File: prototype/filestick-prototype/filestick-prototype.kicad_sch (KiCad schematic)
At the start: 60 parts, among them J1 DIN-5, J2 DIN-5, J3 GPIO header 1, J4 UART header, J5 GPIO header 2, J6 SPI header, Q1 2N7002, Q2 2N7002, Q3 2N7002, Q4 2N7002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

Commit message: fix prototype PCB errors
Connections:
- net GND: now also U4.42 (GND); no longer U4.41 (GND)
- net MISO: now also J6.6 (Pin_6), U4.45 (GPIO17_MISO); no longer J6.7 (Pin_7), U4.46 (GPIO17_MISO)
- net MOSI: now also J6.7 (Pin_7), U4.46 (GPIO14_MOSI); no longer J6.6 (Pin_6), U4.45 (GPIO14_MOSI)
- net at TP3.1 (Pin_1): now also U4.41 (CLK_12MHz); no longer U4.42 (CLK_12MHz)
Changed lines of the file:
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@@
-    (stroke (width 0) (type default) (color 0 0 0 0))
-  )
-  (wire (pts (xy 316.23 162.56) (xy 316.23 154.94))
     (stroke (width 0) (type default) (color 0 0 0 0))
   )
@@
     (stroke (width 0) (type default) (color 0 0 0 0))
   )
+  (wire (pts (xy 292.1 158.75) (xy 314.96 158.75))
+    (stroke (width 0) (type default) (color 0 0 0 0))
+  )
   (wire (pts (xy 298.45 215.9) (xy 292.1 215.9))
     (stroke (width 0) (type default) (color 0 0 0 0))
@@
     (stroke (width 0) (type default) (color 0 0 0 0))
   )
-  (wire (pts (xy 321.31 157.48) (xy 327.66 157.48))
-    (stroke (width 0) (type default) (color 0 0 0 0))
-  )
   (wire (pts (xy 359.41 177.8) (xy 365.76 177.8))
     (stroke (width 0) (type default) (color 0 0 0 0))
@@
     (stroke (width 0) (type default) (color 0 0 0 0))
   )
+  (wire (pts (xy 317.5 157.48) (xy 317.5 162.56))
+    (stroke (width 0) (type default) (color 0 0 0 0))
+  )
   (wire (pts (xy 227.33 26.67) (xy 227.33 49.53))
     (stroke (width 0) (type default) (color 0 0 0 0))
@@
     (stroke (width 0) (type default) (color 0 0 0 0))
   )
-  (wire (pts (xy 321.31 158.75) (xy 321.31 157.48))
+  (wire (pts (xy 314.96 154.94) (xy 314.96 158.75))
     (stroke (width 0) (type default) (color 0 0 0 0))
   )
@@
     (stroke (width 0) (type default) (color 0 0 0 0))
   )
-  (wire (pts (xy 316.23 154.94) (xy 327.66 154.94))
-    (stroke (width 0) (type default) (color 0 0 0 0))
-  )
   (wire (pts (xy 81.28 175.26) (xy 81.28 152.4))
     (stroke (width 0) (type default) (color 0 0 0 0))
@@
     (stroke (width 0) (type default) (color 0 0 0 0))
   )
-  (wire (pts (xy 292.1 162.56) (xy 316.23 162.56))
-    (stroke (width 0) (type default) (color 0 0 0 0))
-  )
   (wire (pts (xy 57.15 83.82) (xy 71.12 83.82))
     (stroke (width 0) (type default) (color 0 0 0 0))
@@
     (stroke (width 0) (type default) (color 0 0 0 0))
   )
-  (wire (pts (xy 292.1 158.75) (xy 321.31 158.75))
-    (stroke (width 0) (type default) (color 0 0 0 0))
-  )
   (wire (pts (xy 68.58 185.42) (xy 68.58 180.34))
     (stroke (width 0) (type default) (color 0 0 0 0))
@@
     (stroke (width 0) (type default) (color 0 0 0 0))
   )
+  (wire (pts (xy 292.1 162.56) (xy 317.5 162.56))
+    (stroke (width 0) (type default) (color 0 0 0 0))
+  )
   (wire (pts (xy 110.49 59.69) (xy 105.41 59.69))
     (stroke (width 0) (type default) (color 0 0 0 0))
   )
+  (wire (pts (xy 327.66 157.48) (xy 317.5 157.48))
+    (stroke (width 0) (type default) (color 0 0 0 0))
+  )
   (wire (pts (xy 24.13 80.01) (xy 35.56 80.01))
     (stroke (width 0) (type default) (color 0 0 0 0))
@@
     (stroke (width 0) (type default) (color 0 0 0 0))
   )
+  (wire (pts (xy 314.96 154.94) (xy 327.66 154.94))
+    (stroke (width 0) (type default) (color 0 0 0 0))
+  )
   (wire (pts (xy 219.71 212.09) (xy 250.19 212.09))
     (stroke (width 0) (type default) (color 0 0 0 0))
@@
     (stroke (width 0) (type default) (color 0 0 0 0))
   )
-  (label "MOSI" (at 302.26 162.56 0)
+  (label "MOSI" (at 302.26 158.75 0)
     (effects (font (size 1.27 1.27)) (justify left bottom))
   )
@@
     (effects (font (size 1.27 1.27)) (justify left bottom))
   )
+  (label "MOSI" (at 359.41 180.34 0)
+    (effects (font (size 1.27 1.27)) (justify left bottom))
+  )
   (label "SS3" (at 302.26 177.8 0)
     (effects (font (size 1.27 1.27)) (justify left bottom))
@@
     (effects (font (size 1.27 1.27)) (justify left bottom))
   )
-  (label "MOSI" (at 359.41 182.88 0)
-    (effects (font (size 1.27 1.27)) (justify left bottom))
-  )
   (label "COLLISION_REF_PWM" (at 195.58 58.42 0)
     (effects (font (size 1.27 1.27)) (justify left bottom))
@@
     (effects (font (size 1.27 1.27)) (justify left bottom))
   )
-  (label "MISO" (at 302.26 158.75 0)
-    (effects (font (size 1.27 1.27)) (justify left bottom))
-  )
-  (label "MISO" (at 359.41 180.34 0)
+  (label "MISO" (at 302.26 162.56 0)
     (effects (font (size 1.27 1.27)) (justify left bottom))
   )
@@
     (effects (font (size 1.27 1.27)) (justify left bottom))
   )
+  (label "MISO" (at 359.41 182.88 0)
+    (effects (font (size 1.27 1.27)) (justify left bottom))
+  )

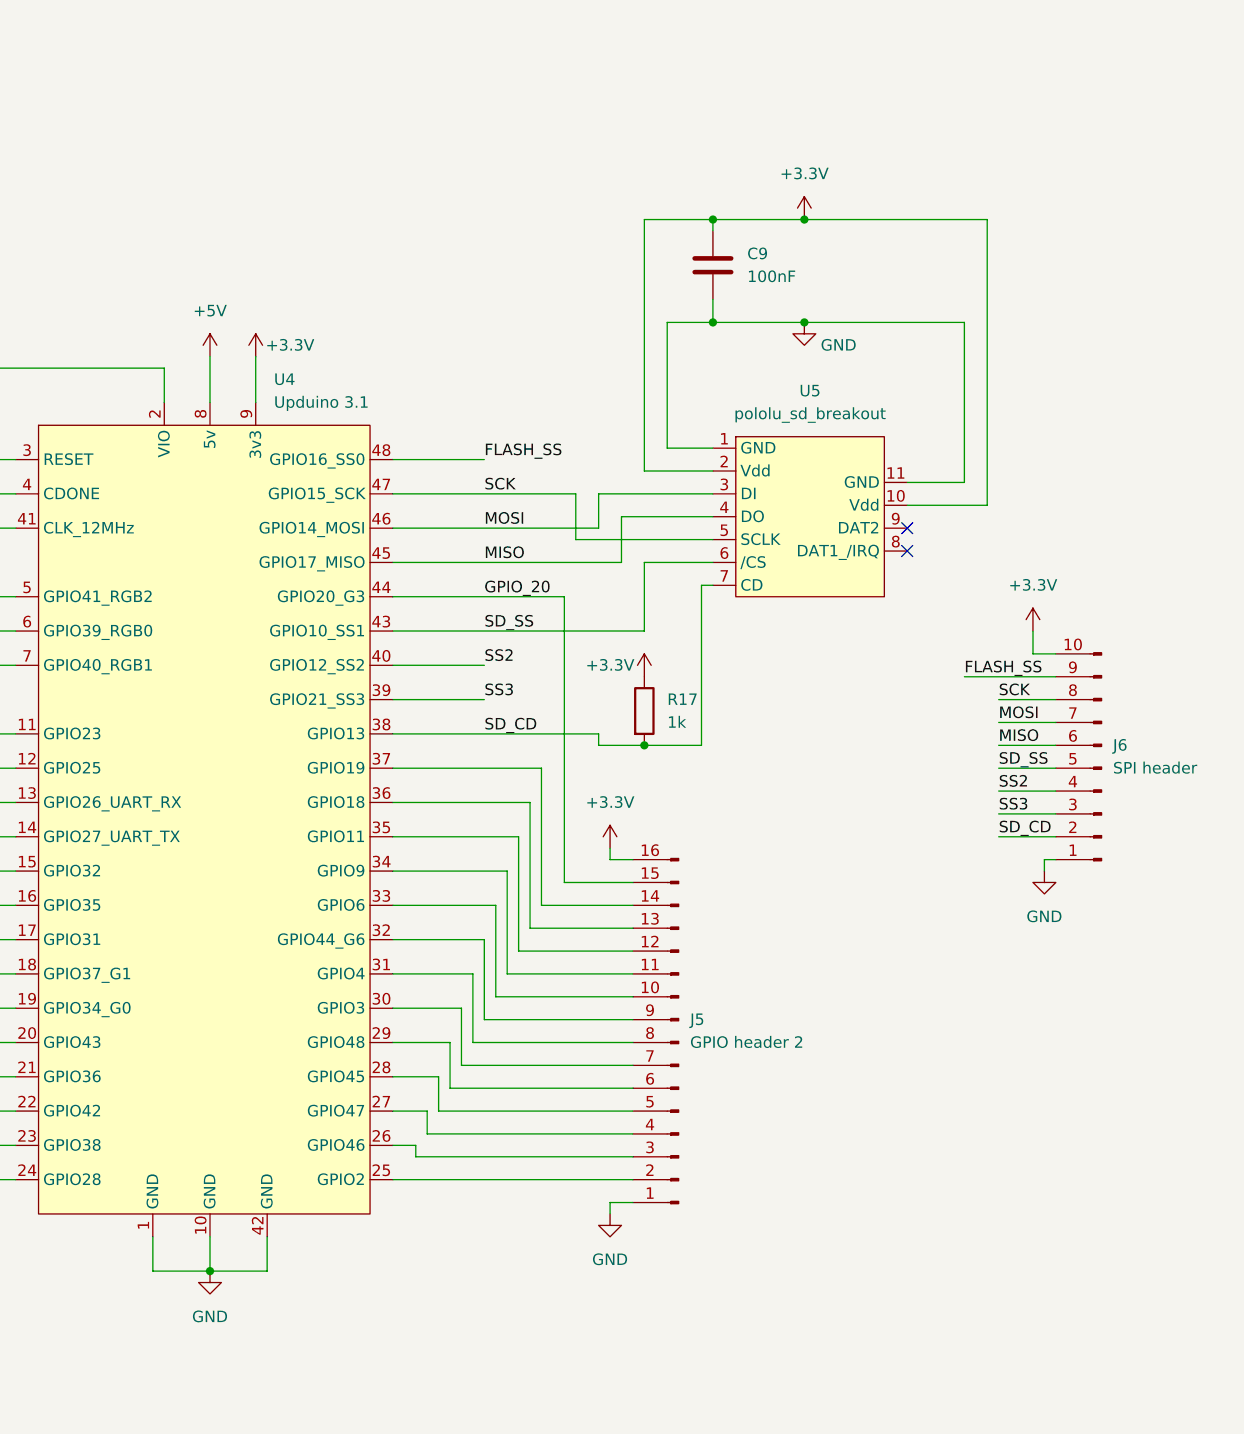
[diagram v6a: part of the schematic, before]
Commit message: Update schematic with dedicated flash spi port
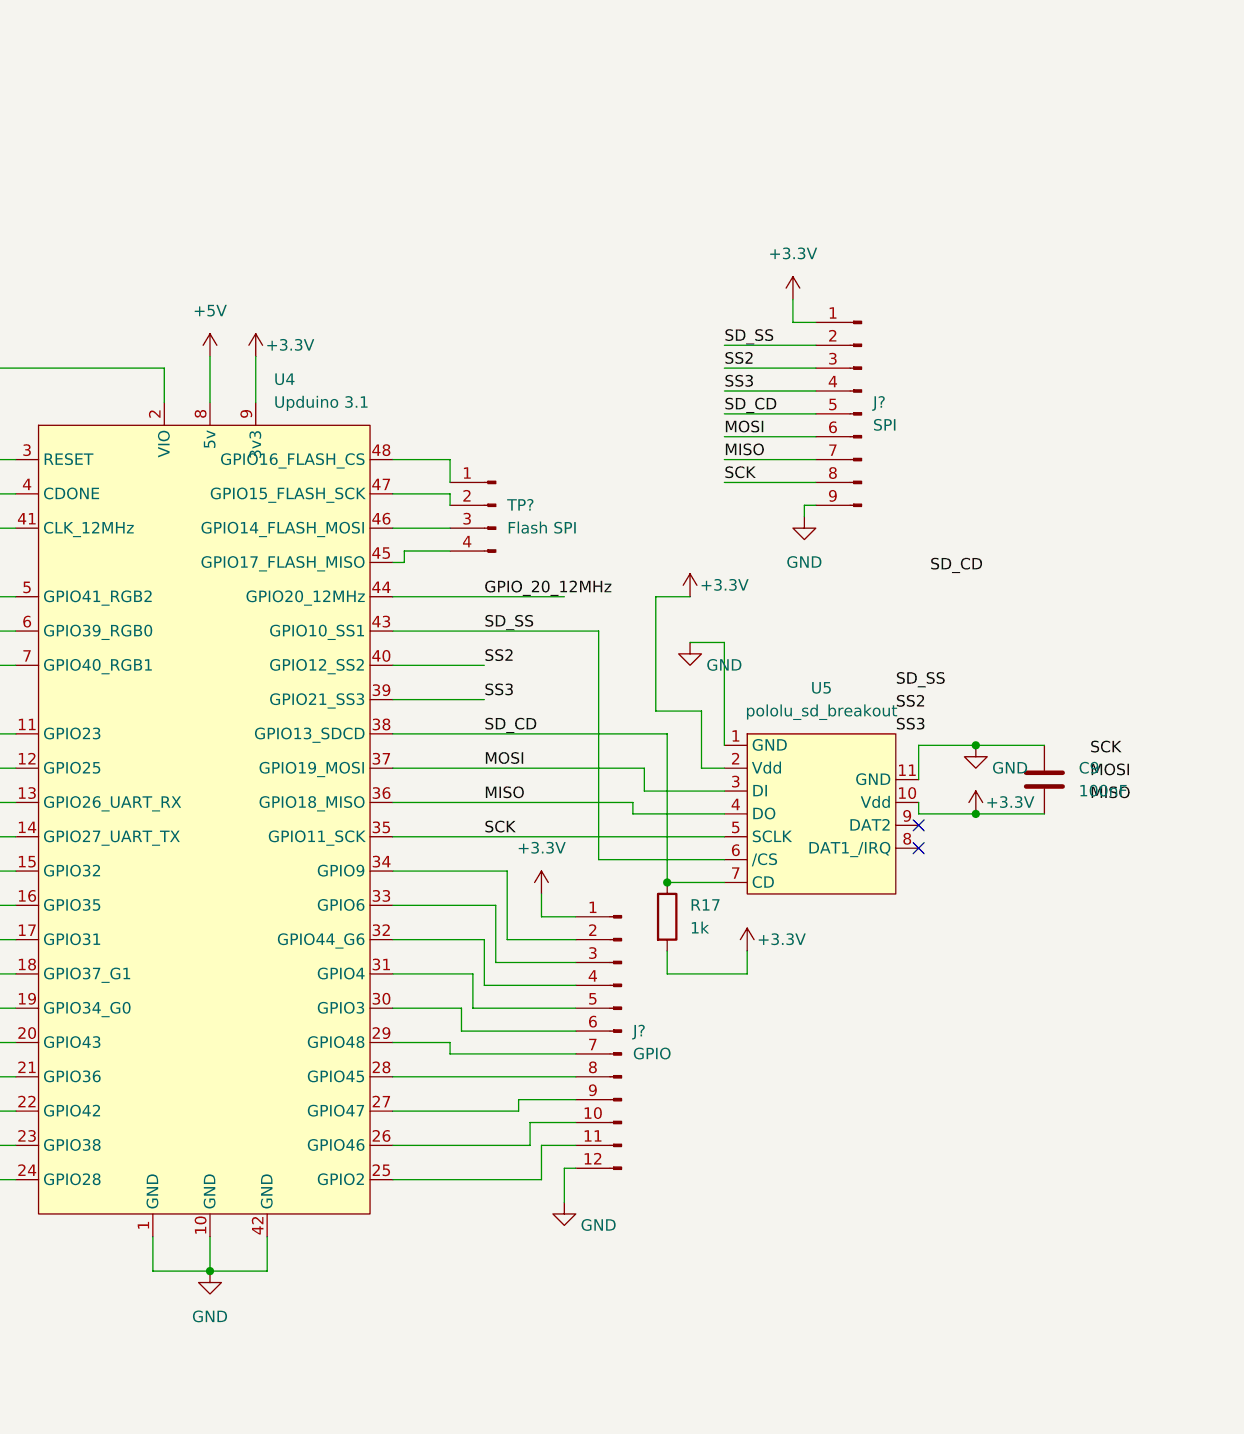
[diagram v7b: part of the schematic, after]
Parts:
- removed J5: GPIO header 2, Connector_PinHeader_2.54mm:PinHeader_1x16_P2.54mm_Vertical, symbol Connector:Conn_01x16_Male
- removed J6: SPI header, Connector_PinHeader_2.54mm:PinHeader_1x10_P2.54mm_Vertical, symbol Connector:Conn_01x10_Male
- added J?: SPI, symbol Connector:Conn_01x09_Male
- added J?: GPIO, symbol Connector:Conn_01x12_Male
- added TP?: Flash SPI, symbol Connector:Conn_01x04_Male
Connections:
- net +3.3V: now also C9.2, R17.2, J?.1 (Pin_1), J?.1 (Pin_1); no longer C9.1, R17.1
- net GND: now also C9.1, J?.12 (Pin_12), J?.9 (Pin_9); no longer C9.2
- net MISO: now also U4.36 (GPIO18_MISO), J?.7 (Pin_7); no longer U4.45 (GPIO17_MISO)
- net MOSI: now also U4.37 (GPIO19_MOSI), J?.6 (Pin_6); no longer U4.46 (GPIO14_MOSI)
- net SCK: now also U4.35 (GPIO11_SCK), J?.8 (Pin_8); no longer U4.47 (GPIO15_SCK)
- net SD_CD: now also R17.1, J?.5 (Pin_5); no longer R17.2
- net SD_SS: now also J?.2 (Pin_2)
- net SS2: now also J?.3 (Pin_3)
- net SS3: now also J?.4 (Pin_4)
- net at U4.25 (GPIO2): now also J?.11 (Pin_11)
- net at U4.26 (GPIO46): now also J?.10 (Pin_10)
- net at U4.27 (GPIO47): now also J?.9 (Pin_9)
- net at U4.28 (GPIO45): now also J?.8 (Pin_8)
- net at U4.29 (GPIO48): now also J?.7 (Pin_7)
- net at U4.30 (GPIO3): now also J?.6 (Pin_6)
- net at U4.31 (GPIO4): now also J?.5 (Pin_5)
- net at U4.32 (GPIO44_G6): now also J?.4 (Pin_4)
- net at U4.33 (GPIO6): now also J?.3 (Pin_3)
- net at U4.34 (GPIO9): now also J?.2 (Pin_2)
- net FLASH_SS: no longer names the net of U4.48 (GPIO16_FLASH_CS)
- net FLASH_SS: now also TP?.1 (Pin_1)
- net GPIO_20 renamed GPIO_20_12MHz
- new net: TP?.4 (Pin_4), U4.45 (GPIO17_FLASH_MISO)
- new net: TP?.3 (Pin_3), U4.46 (GPIO14_FLASH_MOSI)
- new net: TP?.2 (Pin_2), U4.47 (GPIO15_FLASH_SCK)
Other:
- moved on the sheet: C9, R17, U5
